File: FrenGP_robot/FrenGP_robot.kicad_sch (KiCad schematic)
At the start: 19 parts, among them J1 Screw_Terminal_01x02, J2 Screw_Terminal_01x02, J3 Screw_Terminal_01x02, SW1 SW_Push

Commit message: Schematics update
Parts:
- J2: value Screw_Terminal_01x02 -> Right motor
- J3: value Screw_Terminal_01x02 -> Left motor
- R1: value R -> 330R
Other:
- note added: "Arduino Nano"
- note added: "DRV8833 Dual H-bridge"
- note added: "IR line sensors"
- note added: "Power supply"
- note added: "Ultrasonic sensor"
- moved on the sheet: A1, C1, C2, C3, C4, D1, D2, J1, J2, J3, R1, SW1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

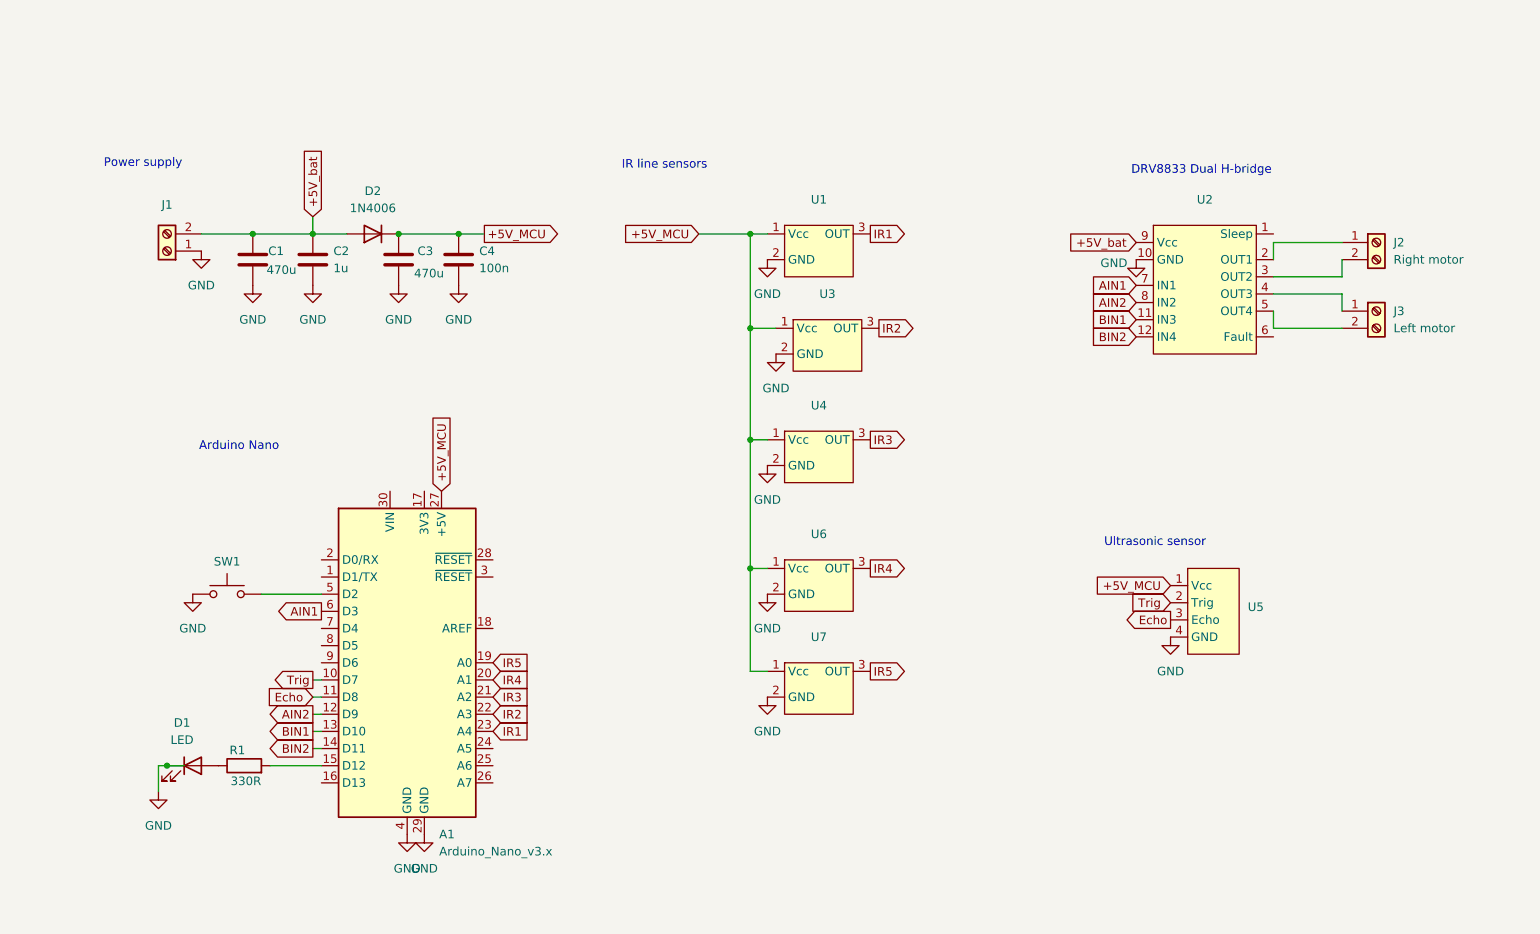
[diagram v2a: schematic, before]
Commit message: Buzzer HC-05 LED blinkers Second pin rows
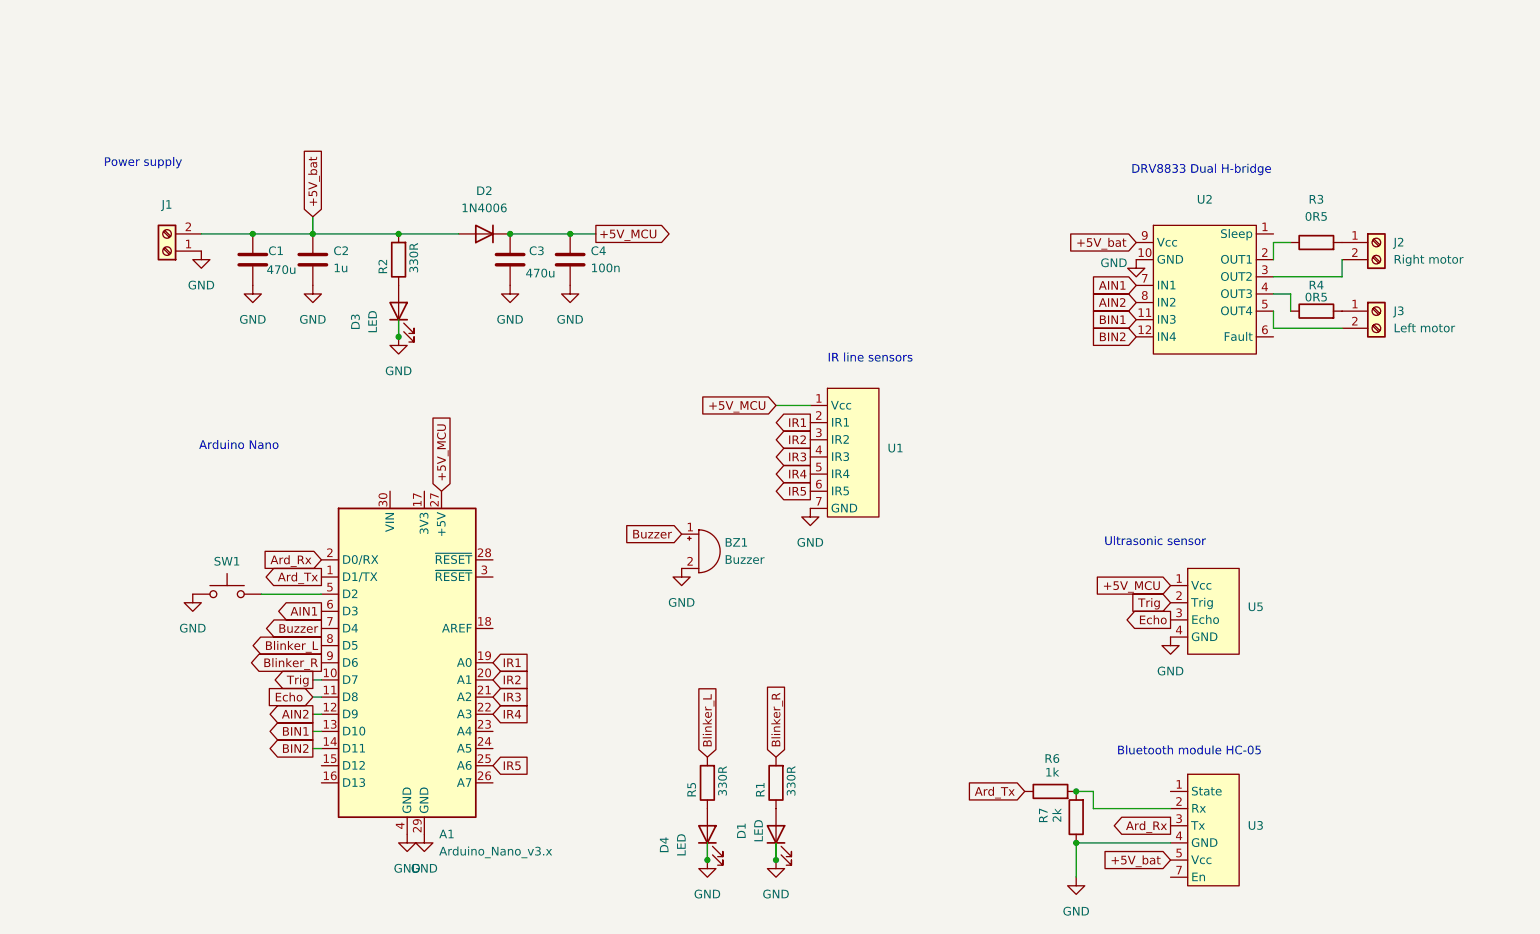
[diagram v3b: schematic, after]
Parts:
- removed U1, U3, U4, U6, U7: ~, DRV_8833_module:3pin_Reflection_sensor, symbol DRV_8833:3pin_reflection_sensor
- added BZ1: Buzzer, Buzzer_Beeper:Buzzer_TDK_PS1240P02BT_D12.2mm_H6.5mm, symbol Device:Buzzer
- added D3, D4: LED, Diode_SMD:D_0603_1608Metric_Pad1.05x0.95mm_HandSolder, symbol Device:LED
- added R2, R5: 330R, Resistor_SMD:R_0603_1608Metric_Pad0.98x0.95mm_HandSolder, symbol Device:R
- added R3, R4: 0R5, Resistor_SMD:R_0805_2012Metric_Pad1.20x1.40mm_HandSolder, symbol Device:R
- added R6: 1k, Resistor_SMD:R_0603_1608Metric_Pad0.98x0.95mm_HandSolder, symbol Device:R
- added R7: 2k, Resistor_SMD:R_0603_1608Metric_Pad0.98x0.95mm_HandSolder, symbol Device:R
- added U1: ~, symbol DRV_8833:5Ch_IR_sensor
- added U3: ~, symbol DRV_8833:HC-05
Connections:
- net +5V_MCU: now also U1.1 (Vcc)
- net +5V_bat: now also R2.2, U3.5 (Vcc)
- net GND: now also BZ1.2 (-), D3.1 (K), D4.1 (K), R7.1, U1.7 (GND), U3.4 (GND)
- net IR1: now also A1.19 (A0), U1.2 (IR1); no longer A1.23 (A4)
- net IR2: now also A1.20 (A1), U1.3 (IR2); no longer A1.22 (A3)
- net IR3: now also U1.4 (IR3)
- net IR4: now also A1.22 (A3), U1.5 (IR4); no longer A1.20 (A1)
- net IR5: now also A1.25 (A6), U1.6 (IR5); no longer A1.19 (A0)
- net at J3.1 (Pin_1): now also R4.2; no longer U2.4 (OUT3)
- net at J2.1 (Pin_1): now also R3.2; no longer U2.2 (OUT1)
- net Ard_Tx: now reaches A1.1 (D1/TX)
- net Ard_Tx: now also R6.1
- net at A1.15 (D12): no longer R1.2
- net Ard_Rx: now reaches A1.2 (D0/RX)
- net Ard_Rx: now also U3.3 (Tx)
- net Buzzer: now reaches A1.7 (D4)
- net Buzzer: now also BZ1.1 (+)
- net Blinker_L: now reaches A1.8 (D5)
- net Blinker_L: now also R5.2
- net Blinker_R: now reaches A1.9 (D6)
- net Blinker_R: now also R1.2
- new net: R4.1, U2.4 (OUT3)
- new net: R6.2, R7.2, U3.2 (Rx)
- new net: R3.1, U2.2 (OUT1)
- new net: D4.2 (A), R5.1
- new net: D3.2 (A), R2.1
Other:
- note added: "Bluetooth module HC-05"
- moved on the sheet: C3, C4, D1, D2, R1

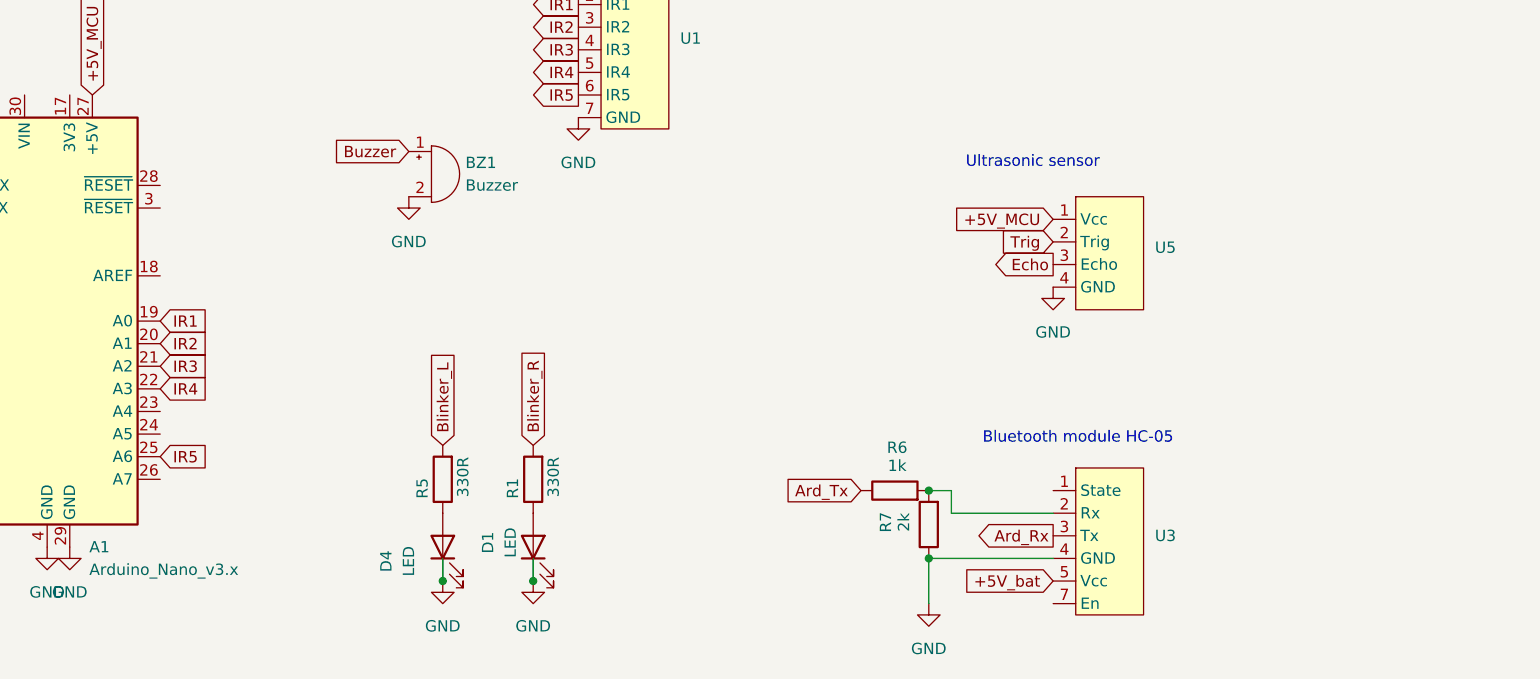
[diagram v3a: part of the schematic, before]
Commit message: Footprints added
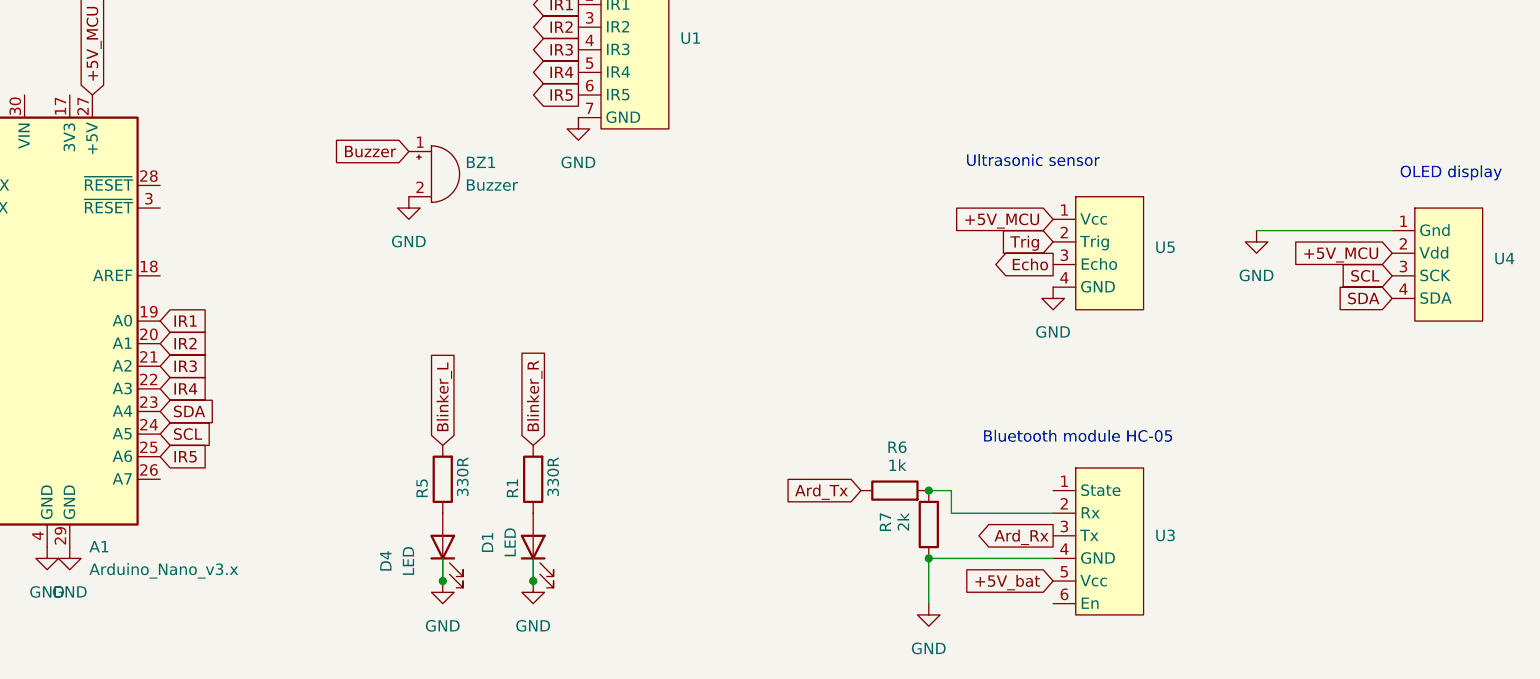
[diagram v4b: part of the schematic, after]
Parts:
- added U4: ~, DRV_8833_module:OLED display header, symbol DRV_8833:OLED_header
- U1: footprint (none) -> DRV_8833_module:IR sensor header
- U3: footprint (none) -> DRV_8833_module:HC-05 header
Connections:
- net +5V_MCU: now also U4.2 (Vdd)
- net GND: now also U4.1 (Gnd)
- net SDA: now reaches A1.23 (A4)
- net SDA: now also U4.4 (SDA)
- net SCL: now reaches A1.24 (A5)
- net SCL: now also U4.3 (SCK)
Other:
- note added: "OLED display"

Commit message: Rev 1.1 finished
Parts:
- BZ1: footprint Buzzer_Beeper:Buzzer_TDK_PS1240P02BT_D12.2mm_H6.5mm -> Buzzer_Beeper:Buzzer_12x9.5RM7.6
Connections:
- net Blinker_L: now also R1.2; no longer R5.2
- net Blinker_R: now also R5.2; no longer R1.2
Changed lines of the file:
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@@
 		)
 	)
-	(global_label "Blinker_R"
+	(global_label "Blinker_L"
 		(shape input)
 		(at 132.08 123.19 90)
@@
 		)
 		(property "Intersheetrefs" "${INTERSHEET_REFS}"
-			(at 132.08 111.3753 90)
+			(at 132.08 111.6172 90)
 			(effects
 				(font
@@
 		)
 	)
-	(global_label "Blinker_L"
+	(global_label "Blinker_R"
 		(shape input)
 		(at 121.92 123.19 90)
@@
 		)
 		(property "Intersheetrefs" "${INTERSHEET_REFS}"
-			(at 121.92 111.6172 90)
+			(at 121.92 111.3753 90)
 			(effects
 				(font
@@
 			)
 		)
-		(property "Footprint" "Buzzer_Beeper:Buzzer_TDK_PS1240P02BT_D12.2mm_H6.5mm"
+		(property "Footprint" "Buzzer_Beeper:Buzzer_12x9.5RM7.6"
 			(at 120.015 90.17 90)
 			(effects
